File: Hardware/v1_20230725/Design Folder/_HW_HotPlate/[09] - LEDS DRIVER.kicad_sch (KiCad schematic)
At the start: 15 parts, among them J901 RCPT_2POS_2.54MM_VERT, J902 RCPT_2POS_2.54MM_VERT, J903 RCPT_2POS_2.54MM_VERT, Q901 AS3400, Q902 AS3400, Q903 AS3400

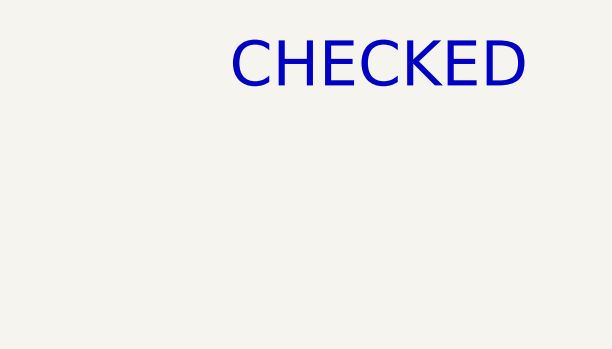
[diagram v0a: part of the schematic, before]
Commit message: Schematic library has been updated
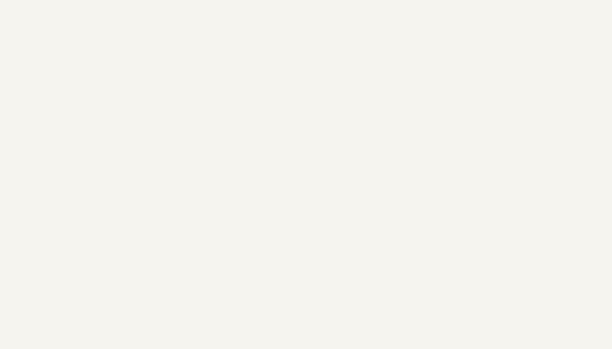
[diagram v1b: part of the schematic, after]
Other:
- note removed: "CHECKED"
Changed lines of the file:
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@@
 (kicad_sch (version 20230121) (generator eeschema)
-  (paper "B")
+  (paper "C")
   (title_block
     (title "Hot Plate")
@@
     (company "Mend0z0")
     (comment 1 "v1")
+    (comment 2 "RELEASED")
     (comment 3 "Siavash Taher Parvar")
     (comment 8 "N/A")
@@
     (effects (font (size 1.27 1.27)) (justify left bottom))
   )
-  (text "CHECKED" (at 382.27 35.56 0)
-    (effects (font (size 5 5)) (justify left bottom))
-  )
   (text "330uA @ +3v3DC" (at 297.18 146.05 0)

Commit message: components have been updated
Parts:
- J901, J902, J903: value RCPT_2POS_2.54MM_VERT -> RECEPT_2X1_VERT_2.54MM; symbol _SCHLIB_HotPlate:CONN_RCPT_2POS_2.54MM_VERT -> _SCHLIB_HotPlate:CONN_RECEPT_2POS_VERT_2.54MM; Manufacturer (none) -> Adam Tech; PCB CHECk (none) -> PCB (N/A); Package (none) -> THD_VERT; Part Number RS1-02-G -> (none); Part Number (Manufacturer) (none) -> RS1-02-G; Part Number (Vendor) (none) -> 2057-RS1-02-G-ND; SCH CHECK CHECKED -> SCH (N/A); Vendor (none) -> Digikey
- Q901, Q902, Q903: symbol _SCHLIB_HotPlate:Q_AS3400 -> _SCHLIB_HotPlate:Q_MOSFET_AS3400_N-CH_30V_5.6A_1.2W_SOT-23-3; Manufacturer (none) -> ANBON SEMICONDUCTOR (INT'L) LIMITED; Max Current 5.6A -> (none); Max P 1.2W -> (none); Max Vds 30V -> (none); PCB CHECk (none) -> PCB (N/A); Part Number AS3400 -> (none); Part Number (Manufacturer) (none) -> AS3400; Part Number (Vendor) (none) -> 4530-AS3400TR-ND; SCH CHECK CHECKED -> SCH (N/A); Vendor (none) -> Digikey
- R701: value 10KR_1/20W -> 10KR_1/20W_1%; symbol _SCHLIB_HotPlate:RES_10KR_1/20W-R0201 -> _SCHLIB_HotPlate:RES_10KR_1/20W_1%_R0201; Manufacturer (none) -> Stackpole Electronics Inc; PCB CHECk (none) -> PCB (N/A); Part Number RMCF0201FT10K0 -> (none); Part Number (Manufacturer) (none) -> RMCF0201FT10K0; Part Number (Vendor) (none) -> RMCF0201FT10K0TR-ND; SCH CHECK CHECKED -> SCH (N/A); Vendor (none) -> Digikey
- R702: value 100R_1/20W -> 100R_1/20W_1%; symbol _SCHLIB_HotPlate:RES_100R_1/20W-R0201 -> _SCHLIB_HotPlate:RES_100R_1/20W_1%_R0201; Manufacturer (none) -> Stackpole Electronics Inc; PCB CHECk (none) -> PCB (N/A); Part Number RMCF0201FT100R -> (none); Part Number (Manufacturer) (none) -> RMCF0201FT100R; Part Number (Vendor) (none) -> RMCF0201FT100RTR-ND; SCH CHECK CHECKED -> SCH (N/A); Vendor (none) -> Digikey
- R901, R902: value 680R_1/8W -> 680R_1/8W_1%; symbol _SCHLIB_HotPlate:RES_680R_1/8W_R0805 -> _SCHLIB_HotPlate:RES_680R_1/8W_1%_R0805; Manufacturer (none) -> YAGEO; PCB CHECk (none) -> PCB (N/A); Part Number AC0805FR-07680RL -> (none); Part Number (Manufacturer) (none) -> AC0805FR-07680RL; Part Number (Vendor) (none) -> 13-AC0805FR-07680RLTR-ND; SCH CHECK CHECKED -> SCH (N/A); Vendor (none) -> Digikey
- R903: value 330R_1/8W -> 330R_1/8W_5%; symbol _SCHLIB_HotPlate:RES_330R_1/8W_R0805 -> _SCHLIB_HotPlate:RES_330R_1/8W_5%_R0805; Manufacturer (none) -> TE Connectivity Passive Product; PCB CHECk (none) -> PCB (N/A); Part Number CRGCQ0805J330R -> (none); Part Number (Manufacturer) (none) -> CRGCQ0805J330R; Part Number (Vendor) (none) -> A130131TR-ND; SCH CHECK CHECKED -> SCH (N/A); Vendor (none) -> Digikey
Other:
- moved on the sheet: J901, J902, J903, Q901, Q902, Q903, R701, R702, R901, R902, R903

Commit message: Updating hardware format structure
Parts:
- Q901, Q902, Q903: footprint Package_TO_SOT_SMD:SOT-23-3 -> Package_TO_SOT_SMD:SOT-23
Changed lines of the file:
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@@
       (effects (font (size 1.27 1.27)) (justify left))
     )
-    (property "Footprint" "Package_TO_SOT_SMD:SOT-23-3" (at 125.73 162.56 0)
+    (property "Footprint" "Package_TO_SOT_SMD:SOT-23" (at 125.73 162.56 0)
       (effects (font (size 1.27 1.27)) (justify left) hide)
     )
@@
       (effects (font (size 1.27 1.27)) (justify left))
     )
-    (property "Footprint" "Package_TO_SOT_SMD:SOT-23-3" (at 450.85 163.83 0)
+    (property "Footprint" "Package_TO_SOT_SMD:SOT-23" (at 450.85 163.83 0)
       (effects (font (size 1.27 1.27)) (justify left) hide)
     )
@@
       (effects (font (size 1.27 1.27)) (justify left))
     )
-    (property "Footprint" "Package_TO_SOT_SMD:SOT-23-3" (at 283.21 162.56 0)
-      (effects (font (size 1.27 1.27)) (justify left) hide)
-    )
+    (property "Footprint" "Package_TO_SOT_SMD:SOT-23" (at 283.21 162.56 0)
+      (effects (font (size 1.27 1.27)) (justify left) hide)
+    )
